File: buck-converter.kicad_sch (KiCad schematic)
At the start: 15 parts, among them J1 Conn_01x02_Socket, J2 Conn_01x02_Socket, J3 Conn_01x02_Socket, J4 Conn_01x02_Socket, U1 TPS562209

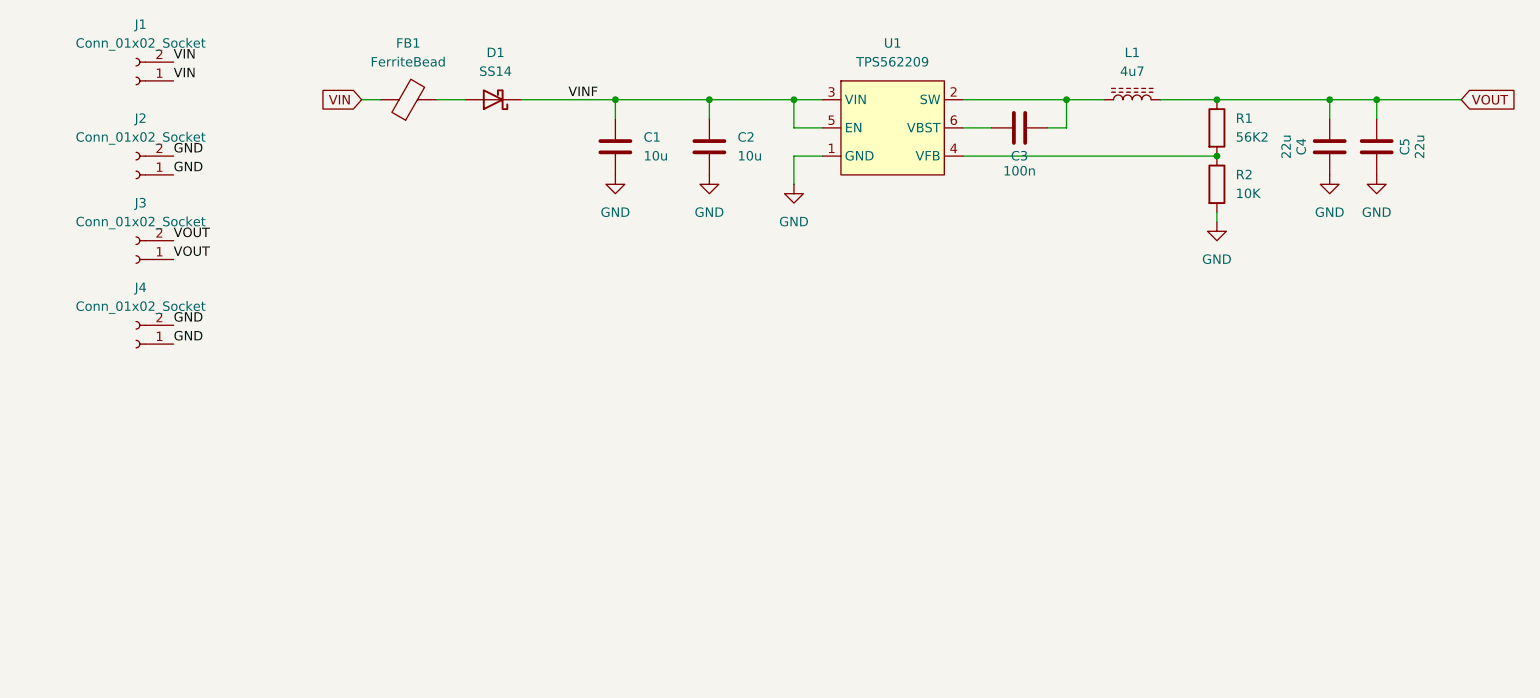
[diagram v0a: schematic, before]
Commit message: ERC fixes
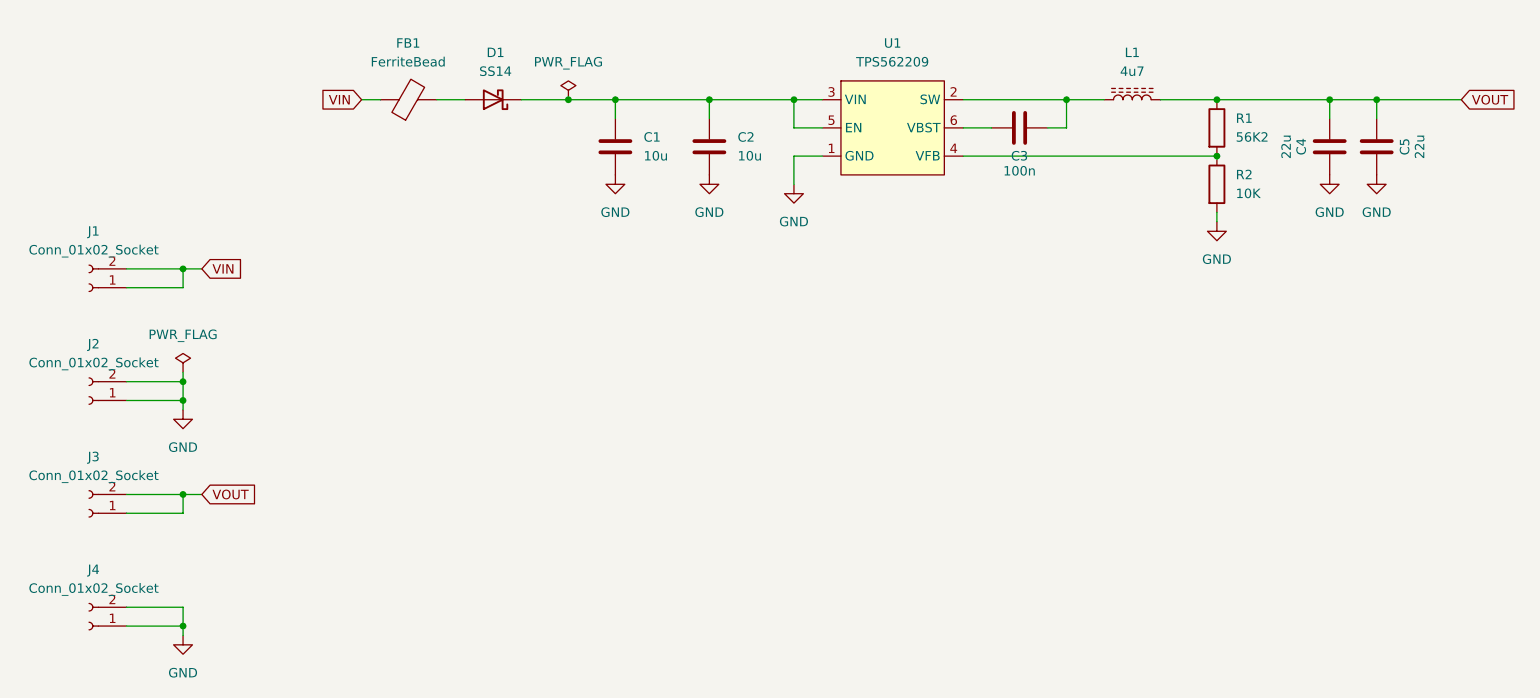
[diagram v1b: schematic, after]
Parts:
- U1: symbol Fijas_Library:TPS562209 -> Regulator_Switching_TI:TPS562209
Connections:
- net VINF: no longer names the net of C1.1, C2.1, D1.1 (K), U1.3 (VIN), U1.5 (EN)
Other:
- moved on the sheet: J1, J2, J3, J4
